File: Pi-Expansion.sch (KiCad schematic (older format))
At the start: 22 parts, among them J1 RPi_GPIO, J2 MMCX_H, J3 PINHEADER_2X2_SMD, P1 BATT, Q1 Q_NPN_BCE, U1 A2200-A, U2 SPX2920U-5.0

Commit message: Documentation update, added notes to schematic.
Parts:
- U2: value SPX2920U-5.0 -> Racom R-78B5.0-1.5L
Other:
- note added: "External Power"
- note added: "GPS A2200-A"
- note added: "GPS status \n indicator"
- note added: "I2C Breakout"
- note added: "Mode selection \njumper"
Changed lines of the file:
@@
 encoding utf-8
 Sheet 1 1
-Title ""
-Date ""
-Rev ""
-Comp ""
+Title "Captain H.Morgan"
+Date "2016-05-22"
+Rev "v1.2"
+Comp "Abersailbot"
 Comment1 ""
 Comment2 ""
@@
 U 1 1 56C0786C
 P 9250 1150
-F 0 "U2" H 9250 1400 50  0000 C CNN
-F 1 "SPX2920U-5.0" H 9250 1350 50  0000 C CNN
+F 0 "U2" H 9250 1450 50  0000 C CNN
+F 1 "Racom R-78B5.0-1.5L" H 9250 1350 50  0000 C CNN
 F 2 "Converters_DCDC_ACDC:DCDC-Conv_Recom_R-78HBxx-0.5" H 9250 1250 50  0001 C CIN
 F 3 "" H 9250 1150 50  0000 C CNN
@@
 Text GLabel 8400 4100 0    55   Input ~ 0
 GPS_TX
+Text Notes 1450 1400 0    60   ~ 0
+Mode selection \njumper
+Text Notes 2750 1500 0    60   ~ 0
+GPS A2200-A
+Text Notes 600  4900 0    60   ~ 0
+I2C Breakout
+Text Notes 8850 700  0    60   ~ 0
+External Power
+Text Notes 8200 4000 0    60   ~ 0
+GPS status \n  indicator
 $EndSCHEMATC

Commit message: Documentation tweaks
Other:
- note added: "Antenna"
- note added: "Raspberry Pi B+\n Header"
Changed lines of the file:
@@
-$EndComp
-$Comp
-L GND #PWR03
-U 1 1 56C036F9
-P 2200 2250
-F 0 "#PWR03" H 2200 2000 50  0001 C CNN
-F 1 "GND" H 2200 2100 50  0000 C CNN
-F 2 "" H 2200 2250 50  0000 C CNN
-F 3 "" H 2200 2250 50  0000 C CNN
-	1    2200 2250
-	1    0    0    -1
 $EndComp
 $Comp
@@
 Text Notes 8200 4000 0    60   ~ 0
 GPS status \n  indicator
+Text Notes 1600 5050 0    60   ~ 0
+Raspberry Pi B+\n       Header
+Text Notes 4200 2150 0    60   ~ 0
+Antenna
 $EndSCHEMATC

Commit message: made minor mods to power supply including moving reverse protection diode from negitive side to positive side to reduce voltage drop.
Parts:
- F1: value FUSE -> POLYFUSE
- JP1: symbol M02X02 -> M02X02-RESCUE-Pi-Expansion
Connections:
- wire segments 82 -> 83
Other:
- moved on the sheet: D1, F1
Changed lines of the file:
@@
 L FUSE F1
 U 1 1 56C2331F
-P 8600 1100
-F 0 "F1" H 8700 1150 50  0000 C CNN
-F 1 "FUSE" H 8500 1050 50  0000 C CNN
-F 2 "Fuse_Holders_and_Fuses:Fuse_SMD1206_HandSoldering" H 8600 1100 50  0001 C CNN
-F 3 "" H 8600 1100 50  0000 C CNN
-	1    8600 1100
-	1    0    0    -1
-$EndComp
-Wire Wire Line
-	8200 1100 8350 1100
+P 8500 1450
+F 0 "F1" H 8600 1500 50  0000 C CNN
+F 1 "POLYFUSE" H 8300 1400 50  0000 C CNN
+F 2 "Fuse_Holders_and_Fuses:Fuse_SMD1206_HandSoldering" H 8500 1450 50  0001 C CNN
+F 3 "" H 8500 1450 50  0000 C CNN
+	1    8500 1450
+	-1   0    0    1
+$EndComp
 Wire Wire Line
 	8100 1450 8100 1100
@@
 	10300 1100 10200 1100
 Wire Wire Line
-	8750 1450 9800 1450
-Wire Wire Line
 	1300 1950 1650 1950
 Wire Wire Line
@@
 L DIODE_SCHOTTKY D1
 U 1 1 573A5A31
-P 8550 1450
-F 0 "D1" H 8550 1550 40  0000 C CNN
-F 1 "DIODE_SCHOTTKY" H 8550 1350 40  0000 C CNN
-F 2 "Diodes_SMD:SOD-323" H 8550 1450 60  0001 C CNN
-F 3 "" H 8550 1450 60  0000 C CNN
-	1    8550 1450
-	-1   0    0    1
-$EndComp
-Wire Wire Line
-	8100 1450 8350 1450
+P 8550 1100
+F 0 "D1" H 8550 1200 40  0000 C CNN
+F 1 "DIODE_SCHOTTKY" H 8550 1000 40  0000 C CNN
+F 2 "Diodes_SMD:SOD-323" H 8550 1100 60  0001 C CNN
+F 3 "" H 8550 1100 60  0000 C CNN
+	1    8550 1100
+	1    0    0    -1
+$EndComp
 Connection ~ 1350 3350
 Wire Wire Line
@@
 NoConn ~ 3400 7100
 $Comp
-L M02X02 JP1
+L M02X02-RESCUE-Pi-Expansion JP1
 U 1 1 573E39CA
 P 850 5300
@@
 Text Notes 4200 2150 0    60   ~ 0
 Antenna
+Wire Wire Line
+	8200 1100 8350 1100
+Wire Wire Line
+	8750 1100 8850 1100
+Wire Wire Line
+	8100 1450 8250 1450
+Wire Wire Line
+	8750 1450 9800 1450
 $EndSCHEMATC

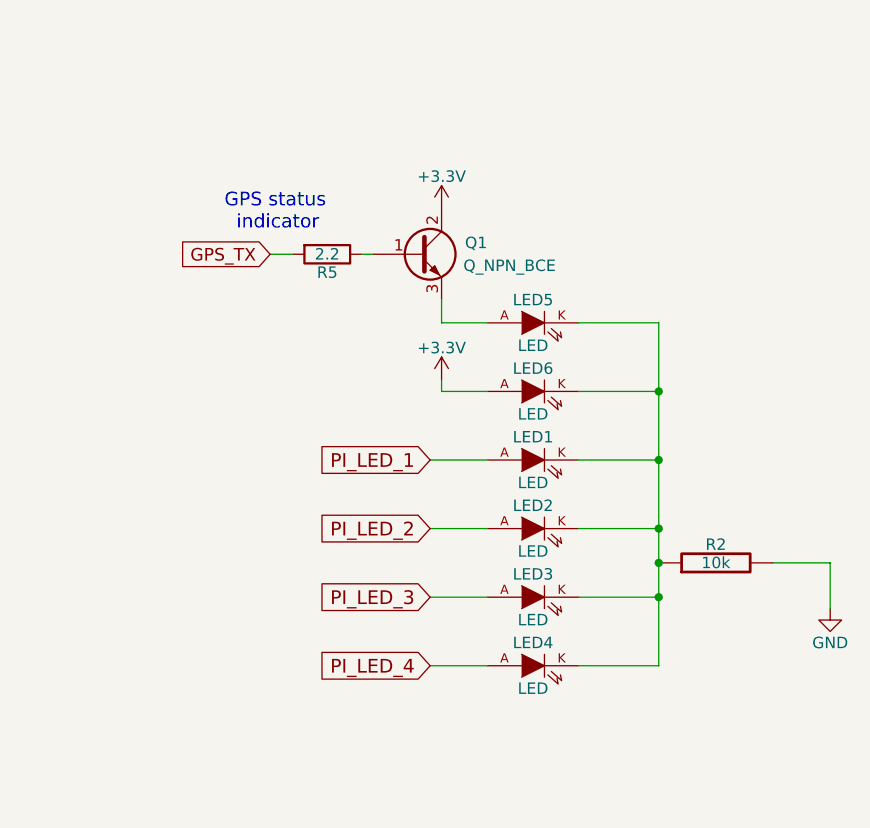
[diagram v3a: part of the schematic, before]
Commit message: cleared out fabrication files as they should be generated fresh when needed, also simplified circuitry for the tx sense led
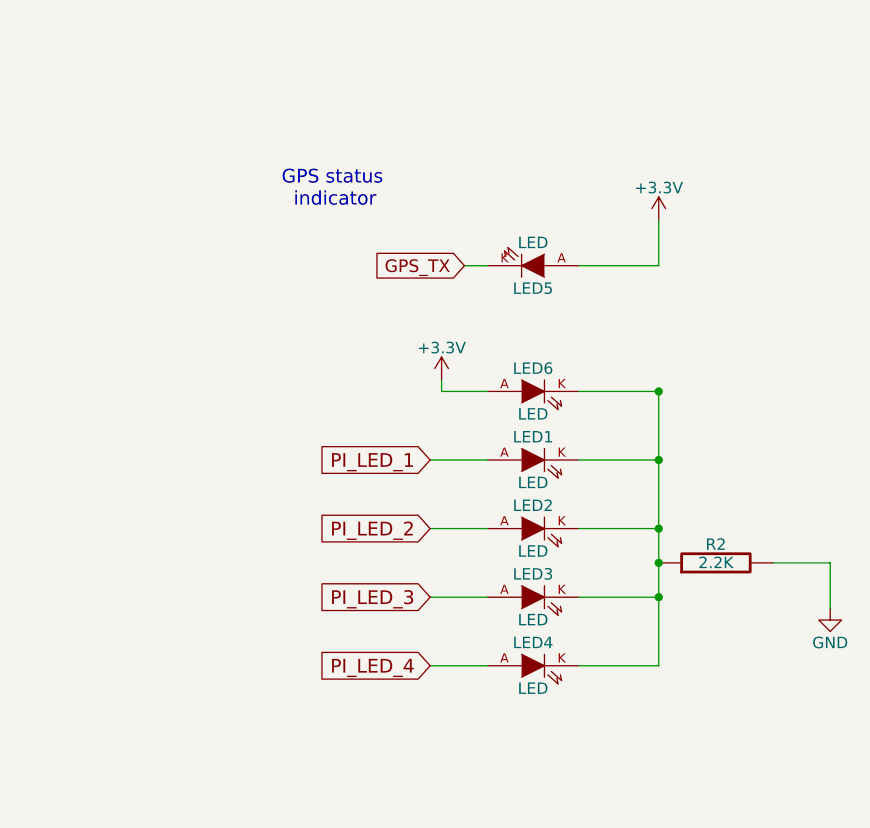
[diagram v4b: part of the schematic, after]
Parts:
- removed Q1: Q_NPN_BCE, TO_SOT_Packages_SMD:SOT-23, symbol Q_NPN_BCE
- removed R5: 2.2, Resistors_SMD:R_1206, symbol R
- R2: value 10k -> 2.2K
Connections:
- net +3V3: now also LED5.A
- net GPS_TX: now also LED5.K
- net at LED1.K, LED2.K, LED3.K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: no longer LED5.K
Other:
- moved on the sheet: LED5
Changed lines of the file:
@@
 P 10350 5450
 F 0 "R2" V 10430 5450 50  0000 C CNN
-F 1 "10k" V 10350 5450 50  0000 C CNN
+F 1 "2.2K" V 10350 5450 50  0000 C CNN
 F 2 "FT:1206" H 10350 5450 60  0001 C CNN
 F 3 "" H 10350 5450 60  0000 C CNN
@@
 	10850 5450 10850 5650
 Wire Wire Line
-	10100 4400 10100 5900
+	10100 4700 10100 5900
 Wire Wire Line
 	10100 5000 9750 5000
@@
 L LED-RESCUE-Pi-Expansion LED5
 U 1 1 573E723E
-P 9550 4400
-F 0 "LED5" H 9550 4500 50  0000 C CNN
-F 1 "LED" H 9550 4300 50  0000 C CNN
-F 2 "FT:LED-1206" H 9550 4400 60  0001 C CNN
-F 3 "" H 9550 4400 60  0000 C CNN
-	1    9550 4400
-	1    0    0    -1
+P 9550 4150
+F 0 "LED5" H 9550 4250 50  0000 C CNN
+F 1 "LED" H 9550 4050 50  0000 C CNN
+F 2 "FT:LED-1206" H 9550 4150 60  0001 C CNN
+F 3 "" H 9550 4150 60  0000 C CNN
+	1    9550 4150
+	-1   0    0    1
 $EndComp
 Wire Wire Line
 	9750 4700 10100 4700
 Connection ~ 10100 5000
-Wire Wire Line
-	9750 4400 10100 4400
 Connection ~ 10100 4700
 $Comp
@@
 Wire Wire Line
 	9150 4700 9350 4700
-Wire Wire Line
-	9350 4400 9150 4400
-Wire Wire Line
-	9150 4400 9150 4300
-$Comp
-L Q_NPN_BCE Q1
-U 1 1 573E7CC9
-P 9050 4100
-F 0 "Q1" H 9350 4150 50  0000 R CNN
-F 1 "Q_NPN_BCE" H 9650 4050 50  0000 R CNN
-F 2 "TO_SOT_Packages_SMD:SOT-23" H 9250 4200 50  0001 C CNN
-F 3 "" H 9050 4100 50  0000 C CNN
-	1    9050 4100
-	1    0    0    -1
-$EndComp
 $Comp
 L +3.3V #PWR019
 U 1 1 573E8084
-P 9150 3900
-F 0 "#PWR019" H 9150 3750 50  0001 C CNN
-F 1 "+3.3V" H 9150 4040 50  0000 C CNN
-F 2 "" H 9150 3900 50  0000 C CNN
-F 3 "" H 9150 3900 50  0000 C CNN
-	1    9150 3900
-	1    0    0    -1
-$EndComp
-$Comp
-L R R5
-U 1 1 573E810F
-P 8650 4100
-F 0 "R5" V 8730 4100 50  0000 C CNN
-F 1 "2.2" V 8650 4100 50  0000 C CNN
-F 2 "Resistors_SMD:R_1206" V 8580 4100 50  0001 C CNN
-F 3 "" H 8650 4100 50  0000 C CNN
-	1    8650 4100
-	0    1    1    0
-$EndComp
-Wire Wire Line
-	8800 4100 8850 4100
-Wire Wire Line
-	8400 4100 8500 4100
-Text GLabel 8400 4100 0    55   Input ~ 0
+P 10100 3950
+F 0 "#PWR019" H 10100 3800 50  0001 C CNN
+F 1 "+3.3V" H 10100 4090 50  0000 C CNN
+F 2 "" H 10100 3950 50  0000 C CNN
+F 3 "" H 10100 3950 50  0000 C CNN
+	1    10100 3950
+	1    0    0    -1
+$EndComp
+Wire Wire Line
+	9250 4150 9350 4150
+Text GLabel 9250 4150 0    55   Input ~ 0
 GPS_TX
 Text Notes 1450 1400 0    60   ~ 0
@@
 Text Notes 8850 700  0    60   ~ 0
 External Power
-Text Notes 8200 4000 0    60   ~ 0
+Text Notes 8450 3900 0    60   ~ 0
 GPS status \n  indicator
 Text Notes 1600 5050 0    60   ~ 0
@@
 Wire Wire Line
 	8750 1450 9800 1450
+Wire Wire Line
+	10100 4150 10100 3950
+Wire Wire Line
+	9750 4150 10100 4150
 $EndSCHEMATC
